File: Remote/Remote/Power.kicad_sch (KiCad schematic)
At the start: 16 parts, among them J1 USB4125-GF-A_REVA2, J2 B2B-XH-A, U1 MCP73831T-2DCI_OT, U2 AP2210N-3.3TRG1

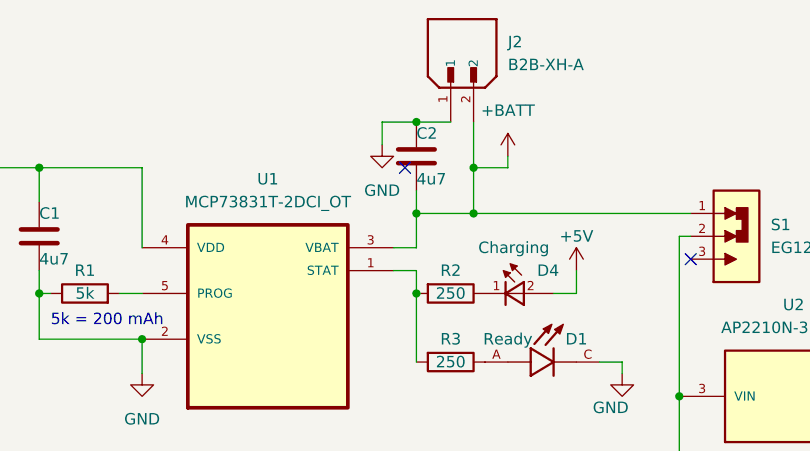
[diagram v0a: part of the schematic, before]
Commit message: Added footprints
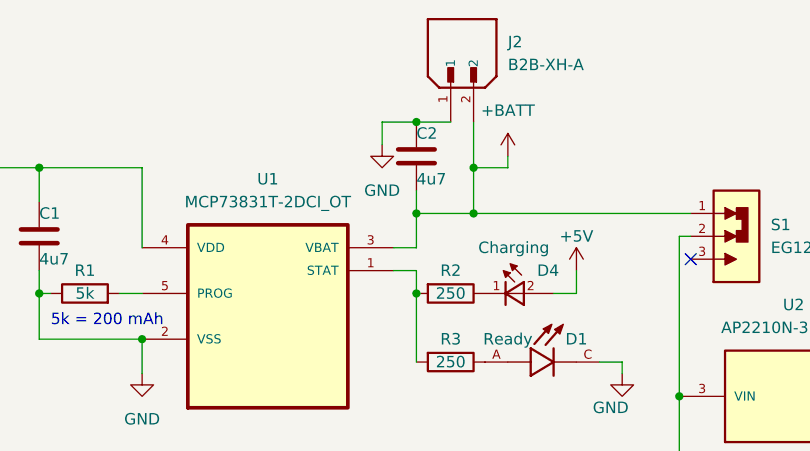
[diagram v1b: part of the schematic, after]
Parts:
- C1, C2, C3, C4: footprint (none) -> Power_:CAPC1608X90N
- R1: footprint (none) -> Power_:RESC3116X65N
- R2, R3: footprint (none) -> Power_:RESC1608X55N
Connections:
- no-connect marks 2 -> 1
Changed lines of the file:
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@@
   (junction (at 36.83 80.01) (diameter 0) (color 0 0 0 0)
   )
-  (no_connect (at 107.95 71.12))
   (no_connect (at 139.7 81.28))
   (wire (pts (xy 36.83 102.87) (xy 36.83 105.41))
@@
       (effects (font (size 1.27 1.27)))
     )
-    (property "Footprint" "" (at 113.03 83.312 90)
-      (effects (font (size 1.27 1.27)) hide)
-    )
-    (property "Datasheet" "~" (at 113.03 85.09 0)
+    (property "Footprint" "Power_:RESC1608X55N" (at 113.03 83.312 90)
+      (effects (font (size 1.27 1.27)) hide)
+    )
+    (property "Datasheet" "RT0603BRE07250RL" (at 113.03 85.09 0)
       (effects (font (size 1.27 1.27)) hide)
     )
@@
       (effects (font (size 1.27 1.27)) (justify left))
     )
-    (property "Footprint" "" (at 68.2752 82.55 0)
-      (effects (font (size 1.27 1.27)) hide)
-    )
-    (property "Datasheet" "~" (at 67.31 78.74 0)
+    (property "Footprint" "Power_:CAPC1608X90N" (at 68.2752 82.55 0)
+      (effects (font (size 1.27 1.27)) hide)
+    )
+    (property "Datasheet" "CL10A475KP8NNNC" (at 67.31 78.74 0)
       (effects (font (size 1.27 1.27)) hide)
     )
@@
       (effects (font (size 1.27 1.27)) (justify left))
     )
-    (property "Footprint" "" (at 110.1852 73.66 0)
+    (property "Footprint" "Power_:CAPC1608X90N" (at 110.1852 73.66 0)
       (effects (font (size 1.27 1.27)) hide)
     )
@@
       (effects (font (size 1.27 1.27)))
     )
-    (property "Footprint" "" (at 72.39 86.868 90)
-      (effects (font (size 1.27 1.27)) hide)
-    )
-    (property "Datasheet" "~" (at 72.39 85.09 0)
+    (property "Footprint" "Power_:RESC3116X65N" (at 72.39 86.868 90)
+      (effects (font (size 1.27 1.27)) hide)
+    )
+    (property "Datasheet" "RT1206BRD075KL" (at 72.39 85.09 0)
       (effects (font (size 1.27 1.27)) hide)
     )
@@
       (effects (font (size 1.27 1.27)))
     )
-    (property "Footprint" "" (at 173.0248 91.44 0)
+    (property "Footprint" "Power_:CAPC1608X90N" (at 173.0248 91.44 0)
       (effects (font (size 1.27 1.27)) hide)
     )
@@
       (effects (font (size 1.27 1.27)))
     )
-    (property "Footprint" "" (at 113.03 90.932 90)
+    (property "Footprint" "Power_:RESC1608X55N" (at 113.03 90.932 90)
       (effects (font (size 1.27 1.27)) hide)
     )
@@
       (effects (font (size 1.27 1.27)))
     )
-    (property "Footprint" "" (at 153.67 105.7148 0)
-      (effects (font (size 1.27 1.27)) hide)
-    )
+    (property "Footprint" "Power_:CAPC1608X90N" (at 153.67 105.7148 0)
+      (effects (font (size 1.27 1.27)) hide)
+    )

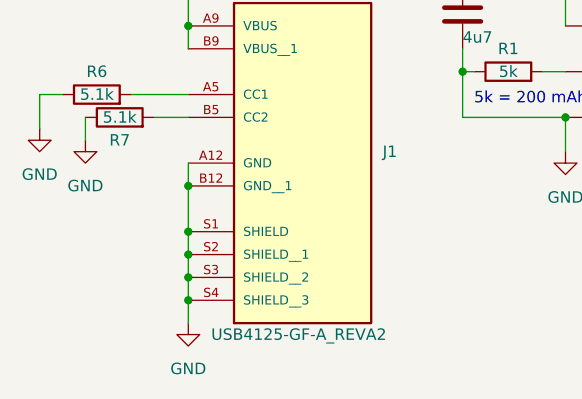
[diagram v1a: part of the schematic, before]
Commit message: Finished with remote V1 PCB
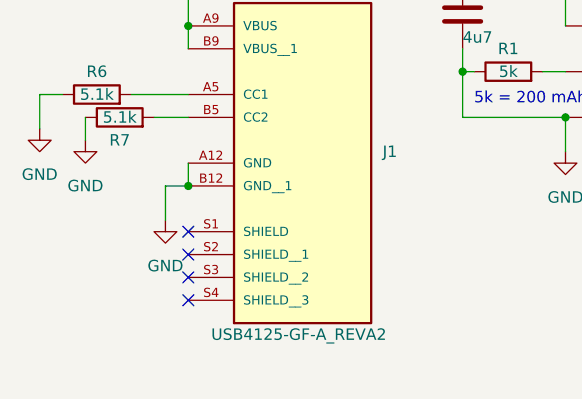
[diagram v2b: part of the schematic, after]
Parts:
- R6, R7: footprint (none) -> Power_:RESC1608X50N
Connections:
- net GND: no longer J1.S1 (SHIELD), J1.S2 (SHIELD__1), J1.S3 (SHIELD__2), J1.S4 (SHIELD__3)
- no-connect marks 1 -> 5
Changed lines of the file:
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@@
   (junction (at 109.22 66.04) (diameter 0) (color 0 0 0 0)
   )
-  (junction (at 36.83 105.41) (diameter 0) (color 0 0 0 0)
-  )
   (junction (at 36.83 71.12) (diameter 0) (color 0 0 0 0)
   )
   (junction (at 115.57 71.12) (diameter 0) (color 0 0 0 0)
   )
-  (junction (at 36.83 110.49) (diameter 0) (color 0 0 0 0)
-  )
-  (junction (at 36.83 102.87) (diameter 0) (color 0 0 0 0)
-  )
   (junction (at 67.31 71.12) (diameter 0) (color 0 0 0 0)
   )
+  (junction (at 36.83 97.79) (diameter 0) (color 0 0 0 0)
+  )
   (junction (at 115.57 76.2) (diameter 0) (color 0 0 0 0)
   )
   (junction (at 67.31 85.09) (diameter 0) (color 0 0 0 0)
   )
-  (junction (at 36.83 107.95) (diameter 0) (color 0 0 0 0)
-  )
   (junction (at 173.99 90.17) (diameter 0) (color 0 0 0 0)
   )
-  (junction (at 36.83 97.79) (diameter 0) (color 0 0 0 0)
-  )
   (junction (at 78.74 90.17) (diameter 0) (color 0 0 0 0)
   )
   (junction (at 36.83 80.01) (diameter 0) (color 0 0 0 0)
   )
+  (no_connect (at 36.83 107.95))
+  (no_connect (at 36.83 102.87))
+  (no_connect (at 36.83 105.41))
   (no_connect (at 139.7 81.28))
-  (wire (pts (xy 36.83 102.87) (xy 36.83 105.41))
-    (stroke (width 0) (type default))
-  )
+  (no_connect (at 36.83 110.49))
   (wire (pts (xy 146.05 106.68) (xy 138.43 106.68))
     (stroke (width 0) (type default))
@@
     (stroke (width 0) (type default))
   )
-  (wire (pts (xy 36.83 110.49) (xy 36.83 113.03))
-    (stroke (width 0) (type default))
-  )
   (wire (pts (xy 36.83 95.25) (xy 36.83 97.79))
     (stroke (width 0) (type default))
@@
     (stroke (width 0) (type default))
   )
-  (wire (pts (xy 36.83 107.95) (xy 36.83 110.49))
-    (stroke (width 0) (type default))
-  )
   (wire (pts (xy 173.99 99.06) (xy 167.64 99.06))
     (stroke (width 0) (type default))
@@
     (stroke (width 0) (type default))
   )
-  (wire (pts (xy 36.83 105.41) (xy 36.83 107.95))
+  (wire (pts (xy 34.29 97.79) (xy 36.83 97.79))
     (stroke (width 0) (type default))
   )
@@
     (stroke (width 0) (type default))
   )
-  (wire (pts (xy 36.83 97.79) (xy 36.83 102.87))
-    (stroke (width 0) (type default))
-  )
   (wire (pts (xy 78.74 90.17) (xy 78.74 93.98))
     (stroke (width 0) (type default))
@@
   )
   (wire (pts (xy 109.22 66.04) (xy 113.03 66.04))
+    (stroke (width 0) (type default))
+  )
+  (wire (pts (xy 34.29 97.79) (xy 34.29 101.6))
     (stroke (width 0) (type default))
   )
@@
     )
   )
-  (symbol (lib_id "power:GND") (at 36.83 113.03 0) (unit 1)
-    (in_bom yes) (on_board yes) (dnp no) (fields_autoplaced)
-    (property "Reference" "#PWR01" (at 36.83 119.38 0)
-      (effects (font (size 1.27 1.27)) hide)
-    )
-    (property "Value" "GND" (at 36.83 118.11 0)
-      (effects (font (size 1.27 1.27)))
-    )
-    (property "Footprint" "" (at 36.83 113.03 0)
-      (effects (font (size 1.27 1.27)) hide)
-    )
-    (property "Datasheet" "" (at 36.83 113.03 0)
-      (effects (font (size 1.27 1.27)) hide)
-    )
-    (pin "1")
-    (instances
-      (project "Remote"
-        (path "/b4382ef4-8540-4cf0-8bf7-60a21f991ddf/d6ef35f0-db14-4fb6-a886-f39262892cda"
-          (reference "#PWR01") (unit 1)
-        )
-      )
-    )
-  )
   (symbol (lib_id "Device:R") (at 26.67 87.63 90) (unit 1)
     (in_bom yes) (on_board yes) (dnp no)
@@
       (effects (font (size 1.27 1.27)))
     )
-    (property "Footprint" "" (at 26.67 89.408 90)
-      (effects (font (size 1.27 1.27)) hide)
-    )
-    (property "Datasheet" "~" (at 26.67 87.63 0)
+    (property "Footprint" "Power_:RESC1608X50N" (at 26.67 89.408 90)
+      (effects (font (size 1.27 1.27)) hide)
+    )
+    (property "Datasheet" "RR0816P-512-D" (at 26.67 87.63 0)
       (effects (font (size 1.27 1.27)) hide)
     )
@@
       (effects (font (size 1.27 1.27)))
     )
-    (property "Footprint" "" (at 29.21 91.948 90)
+    (property "Footprint" "Power_:RESC1608X50N" (at 29.21 91.948 90)
       (effects (font (size 1.27 1.27)) hide)
     )
@@
         )
       )
+    )
+  )
+  (symbol (lib_id "power:GND") (at 34.29 101.6 0) (unit 1)
+    (in_bom yes) (on_board yes) (dnp no) (fields_autoplaced)
+    (property "Reference" "#PWR01" (at 34.29 107.95 0)
+      (effects (font (size 1.27 1.27)) hide)
+    )
+    (property "Value" "GND" (at 34.29 106.68 0)
+      (effects (font (size 1.27 1.27)))
+    )
+    (property "Footprint" "" (at 34.29 101.6 0)
+      (effects (font (size 1.27 1.27)) hide)
+    )
+    (property "Datasheet" "" (at 34.29 101.6 0)
+      (effects (font (size 1.27 1.27)) hide)
+    )
+    (pin "1")
+    (instances
+      (project "Remote"
+        (path "/b4382ef4-8540-4cf0-8bf7-60a21f991ddf/d6ef35f0-db14-4fb6-a886-f39262892cda"
+          (reference "#PWR01") (unit 1)
+        )
+      )
